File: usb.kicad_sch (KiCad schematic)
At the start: 127 parts, among them J3 USB4105-GF-A, J4 WE_632723300011_alt_symbol, Q1 NX138BKMYL, Q2 NX138BKMYL, Q3 NX138BKMYL, U10 TUSB1046-DCI, U11 TPD4E05U06QDQARQ1, U12 AP22615, U13 TPD4E05U06QDQARQ1, U14 TPD4E05U06QDQARQ1, U15 TPD4E05U06QDQARQ1, U16 TPD4E05U06QDQARQ1, U5 FT230XQ-R, U6 TPS65988, U7 W25Q80DVUXIE_TR, U8 TPS7B8133DRVR, U9 AP22615

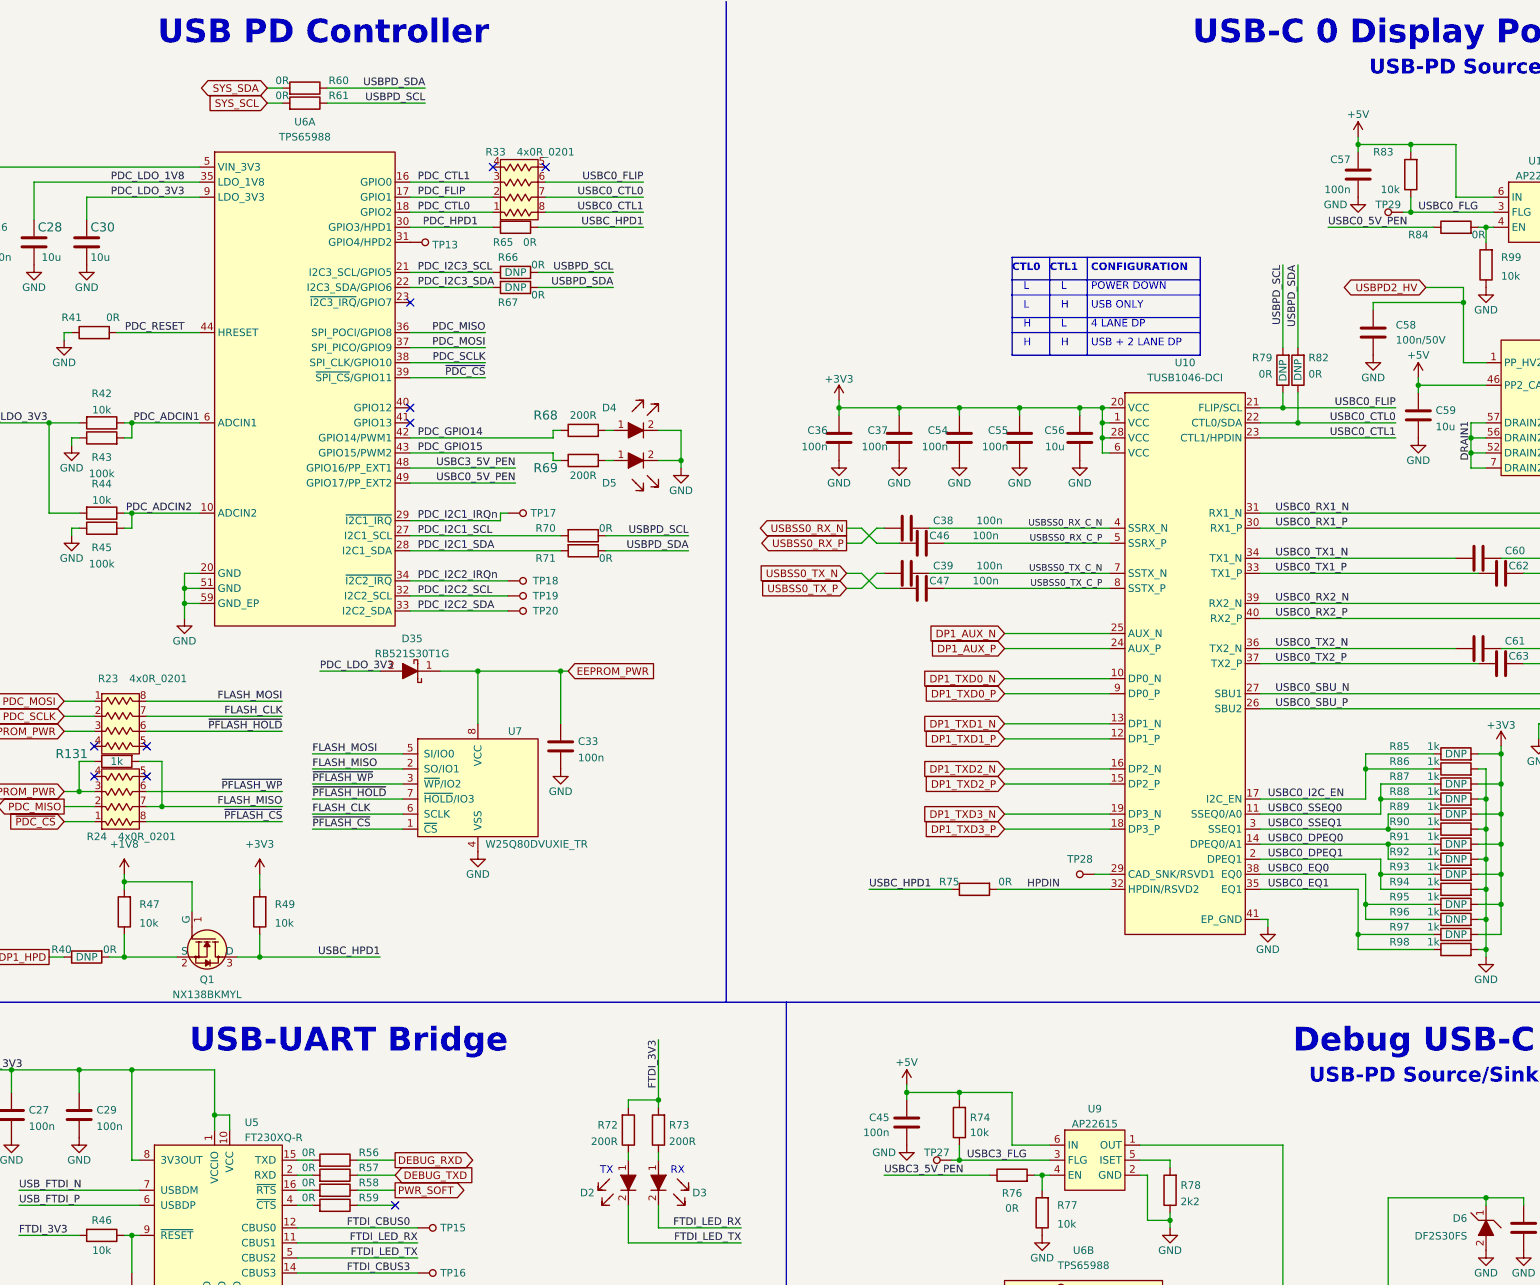
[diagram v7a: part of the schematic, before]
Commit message: CSchematic changes after review
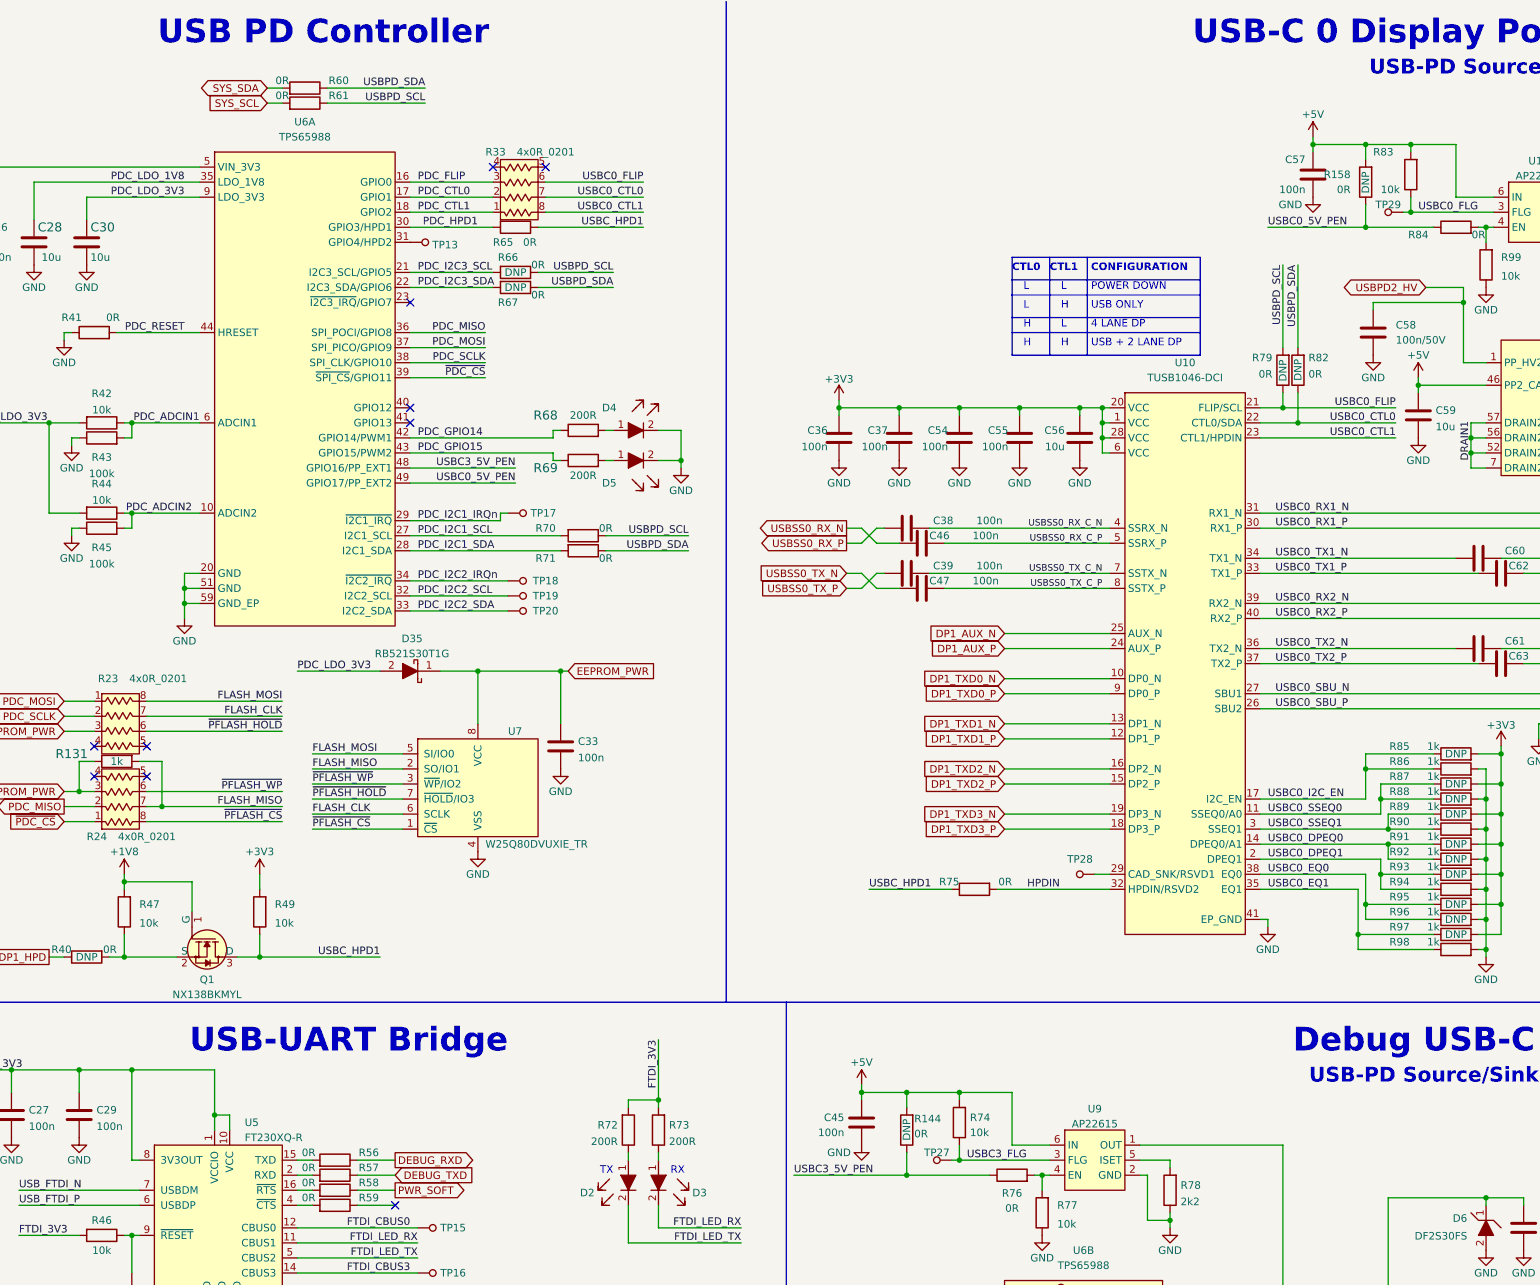
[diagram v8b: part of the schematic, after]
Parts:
- added R144, R158: R_0R_0402, antmicro-footprints:0402-res, symbol antmicroResistors0402:R_0R_0402
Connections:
- net +5V: now also R144.2, R158.2
- net PDC_CTL0: now also R33.2, U6.17 (GPIO1); no longer R33.1, U6.18 (GPIO2)
- net PDC_CTL1: now also R33.1, U6.18 (GPIO2); no longer R33.3, U6.16 (GPIO0)
- net PDC_FLIP: now also R33.3, U6.16 (GPIO0); no longer R33.2, U6.17 (GPIO1)
- net USBC0_5V_PEN: now also R158.1
- net USBC3_5V_PEN: now also R144.1
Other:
- moved on the sheet: C45, C57
